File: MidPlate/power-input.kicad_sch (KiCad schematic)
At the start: 15 parts, among them J1 XT60, J2 XT60, J3 RA1H1C112R, Q1 MCU60P04-TP, Q2 MCU60P04-TP, U1 LM2576

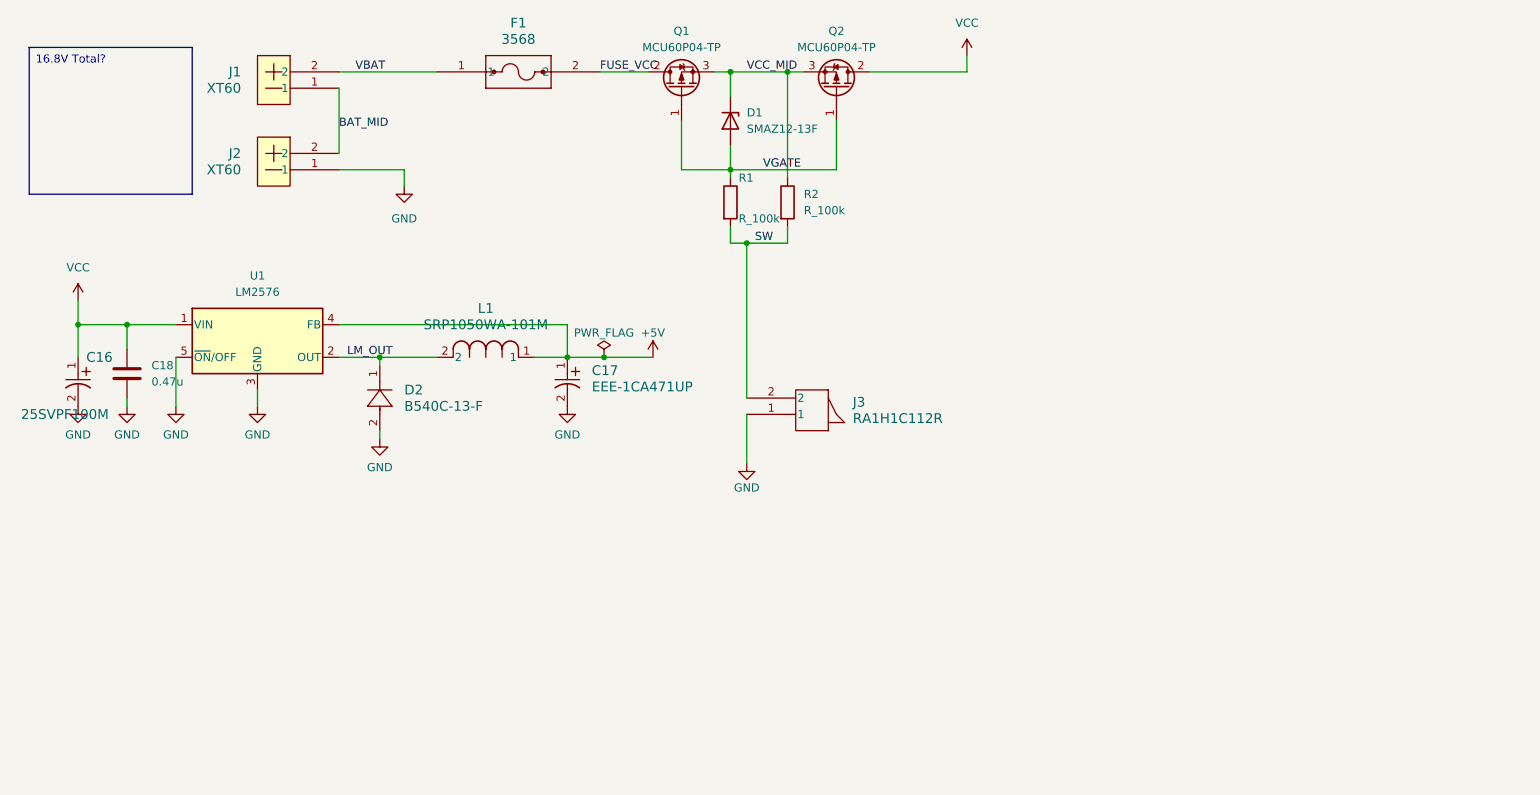
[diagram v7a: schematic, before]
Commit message: update to midplate and powerboard
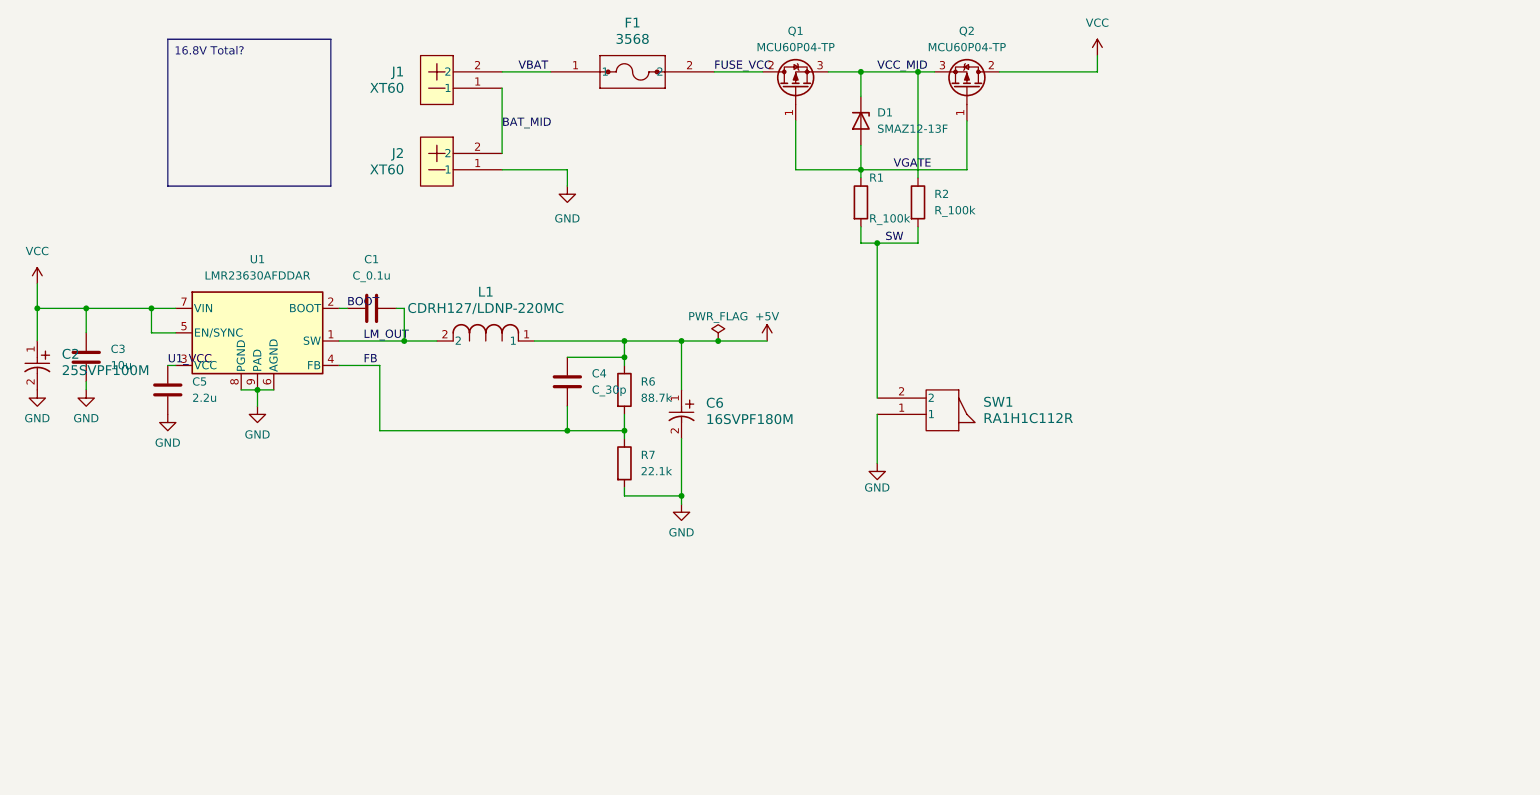
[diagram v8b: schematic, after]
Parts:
- removed C16: 25SVPF100M, bots:PCAP_SVP_E7_PAN, symbol bots:25SVPF100M
- removed C17: EEE-1CA471UP, bots:CAP_EEE_F_PAN, symbol bots:EEE-1CA471UP
- removed C18: 0.47u, bots:C_1206_3216Metric, symbol bots:C_0.47u
- removed D2: B540C-13-F, bots:SMC_DIO, symbol bots:B540C-13-F
- removed L1: SRP1050WA-101M, bots:SRP1050WA-101M, symbol bots:SRP1050WA-101M
- removed U1: LM2576, bots:TO-263-5_TabPin3_LM2576, symbol bots:LM2576
- added C1: C_0.1u, bots:C_0603_1608Metric, symbol bots:C_0.1u
- added C2: 25SVPF100M, bots:CAP_25SVPF100M, symbol bots:25SVPF100M
- added C3: 10u, bots:C_0805_2012Metric, symbol bots:C_10u_1206
- added C4: C_30p, bots:C_0603_1608Metric, symbol bots:C_30p
- added C5: 2.2u, bots:C_0603_1608Metric, symbol bots:C_2.2u
- added C6: 16SVPF180M, bots:CAP_16SVPF180M, symbol bots:16SVPF180M
- added L1: CDRH127/LDNP-220MC, bots:IND_CDRH127_LDNP-470MC_SUM, symbol bots:CDRH127/LDNP-220MC
- added R6: 88.7k, bots:R_0603_1608Metric, symbol bots:R_88.7k
- added R7: 22.1k, bots:R_0603_1608Metric, symbol bots:R_22.1k
- added U1: LMR23630AFDDAR, bots:TI_SO-PowerPAD-8_ThermalVias, symbol bots:LMR23630AFDDAR
- renumbered J3 to SW1
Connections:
- net +5V: now also C4.1, C6.1, L1.1, R6.1
- net GND: now also C2.2, C3.2, C5.2, C6.2, R7.2, U1.6 (AGND), U1.8 (PGND), U1.9 (PAD)
- net LM_OUT: now also C1.2, L1.2, U1.1 (SW)
- net VCC: now also C2.1, C3.1, U1.5 (EN/SYNC), U1.7 (VIN)
- new net BOOT: C1.1, U1.2 (BOOT)
- new net FB: C4.2, R6.2, R7.1, U1.4 (FB)
- new net U1_VCC: C5.1, U1.3 (VCC)
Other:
- moved on the sheet: D1, F1, J1, J2, Q1, Q2, R1, R2, SW1
